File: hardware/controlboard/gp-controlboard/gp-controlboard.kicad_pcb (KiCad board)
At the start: 2 copper layers, 120 x 50 mm, 11 parts

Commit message: .
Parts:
- removed the VAL** at (145.0, 95.0)
- added VAL**: BUTTON-WE-430162073826, BUTTON:BUTTON-WE-430162073826, F.Cu at (110.0, 110.0)
- added VAL**: BUTTON-WE-430162073826, BUTTON:BUTTON-WE-430162073826, F.Cu at (150.0, 95.0)
- added VAL**: BUTTON-WE-430162073826, BUTTON:BUTTON-WE-430162073826, F.Cu at (150.0, 110.0)
- added VAL**: BUTTON-WE-430162073826, BUTTON:BUTTON-WE-430162073826, F.Cu at (110.0, 80.0)
- added VAL**: BUTTON-WE-430162073826, BUTTON:BUTTON-WE-430162073826, F.Cu at (150.0, 80.0)
- moved VAL** 20.0 mm to (205.0, 80.0)
- moved VAL** 20.0 mm to (225.0, 110.0)
- moved VAL** 20.0 mm to (225.0, 95.0)
- moved VAL** 20.0 mm to (225.0, 80.0)
- moved VAL** 20.0 mm to (205.0, 110.0)
- moved VAL** 20.0 mm to (205.0, 95.0)
- moved REF** 8.56 mm to (173.6, 79.7)
- moved VAL** 5.00 mm to (110.0, 95.0)
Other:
- board size 120 x 50 mm -> 140 x 50 mm

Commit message: Started PCB
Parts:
- removed REF**: ESP32-WROOM-32D, WIFI:ESP32-WROOM-32D
- added C101: 4u7, CAPACITOR:CAPACITOR-1206, F.Cu at (-79.5, 44.5)
- added C102: 4u7, CAPACITOR:CAPACITOR-1206, F.Cu at (-18.7, 16.3)
- added C103: 1u, CAPACITOR:CAPACITOR-1206, F.Cu at (-24.1, 16.3)
- added C104: 1u, CAPACITOR:CAPACITOR-1206, F.Cu at (-29.6, 16.3)
- added C105: 100n, CAPACITOR:CAPACITOR-0805, F.Cu at (-31.2, 40.7)
- added C106: 10u, CAPACITOR:CAPACITOR-1206, F.Cu at (-74.0, 44.5)
- added C107: 100n, CAPACITOR:CAPACITOR-0805, F.Cu at (-8.47, 17.2)
- added C108: 100n, CAPACITOR:CAPACITOR-0805, F.Cu at (3.18, 5.13)
- added D101: MBRA340T3G, DIODE:DIODE-DO214AC-UNI, F.Cu at (-92.4, 44.9)
- added DL101: GREEN, LEDs:LED-0805, F.Cu at (-1.07, 2.08)
- added DL102: RED, LEDs:LED-0805, F.Cu at (-12.1, 14.2)
- added DL103: RED, LEDs:LED-0805, F.Cu at (-31.2, 34.6)
- added DL104: GREEN, LEDs:LED-0805, F.Cu at (-12.1, 11.1)
- added P101: BATTERY, CONNECTOR_MPT:CONN-MPT0.5_2-2.54, F.Cu at (190.0, 134.0)
- added P102: EN_JMP, CONNECTOR:CONN-STRIP-2x1-2.54, F.Cu at (-66.1, 11.7)
- added P103: NUCLEO-CN3, CONNECTOR:SOCKET_16x1_2.54_SMD-WE-61001611921, F.Cu at (183.0, 115.0)
- added P104: NUCLEO-CN4, CONNECTOR:SOCKET_16x1_2.54_SMD-WE-61001611921, F.Cu at (167.8, 115.0)
- added P105: ESP_PROG, CONNECTOR:CONN-STRIP-3x1-2.54, F.Cu at (-100.9, 44.8)
- added P106: BOOT_JMP, CONNECTOR:CONN-STRIP-2x1-2.54, F.Cu at (-66.1, 15.8)
- added R101: 330, RESISTOR:RESISTOR-0805, F.Cu at (-13.1, 21.5)
- added R102: 270, RESISTOR:RESISTOR-0805, F.Cu at (-7.27, 14.2)
- added R103: 270, RESISTOR:RESISTOR-0805, F.Cu at (-3.02, 11.1)
- added R104: TBD, RESISTOR:RESISTOR-0805, F.Cu at (-26.9, 37.7)
- added R105: 330, RESISTOR:RESISTOR-0805, F.Cu at (-31.2, 37.7)
- added R106: 10k, RESISTOR:RESISTOR-0805, F.Cu at (-26.3, 34.6)
- added R107: TBD, RESISTOR:RESISTOR-0805, F.Cu at (-1.07, 5.13)
- added R108: TBD, RESISTOR:RESISTOR-0805, F.Cu at (-7.27, 11.1)
- added SW101: 430162073826, BUTTON:BUTTON-WE-430162073826, F.Cu at (-24.3, 26.1)
- added SW102: 430162073826, BUTTON:BUTTON-WE-430162073826, F.Cu at (-42.3, 40.1)
- added SW103: 430162073826, BUTTON:BUTTON-WE-430162073826, F.Cu at (-5.22, -6.47)
- added SW104: 430162073826, BUTTON:BUTTON-WE-430162073826, F.Cu at (-23.3, 7.58)
- added SW105: 430162073826, BUTTON:BUTTON-WE-430162073826, F.Cu at (-42.3, 26.1)
- added SW106: 430162073826, BUTTON:BUTTON-WE-430162073826, F.Cu at (-60.4, 40.1)
- added SW107: 430162073826, BUTTON:BUTTON-WE-430162073826, F.Cu at (-23.3, -6.47)
- added SW108: 430162073826, BUTTON:BUTTON-WE-430162073826, F.Cu at (-78.4, 35.7)
- added SW109: 430162073826, BUTTON:BUTTON-WE-430162073826, F.Cu at (-60.4, 26.1)
- added SW110: 430162073826, BUTTON:BUTTON-WE-430162073826, F.Cu at (-96.5, 35.7)
- added SW111: 430162073826, BUTTON:BUTTON-WE-430162073826, F.Cu at (-78.4, 21.7)
- added SW112: 450405020524, SWITCH:SWITCH-SPDT-WURTH-450405020524, F.Cu at (-8.72, 5.08)
- added SW113: 430162073826, BUTTON:BUTTON-WE-430162073826, F.Cu at (-96.5, 21.7)
- added SW114: 430162073826, BUTTON:BUTTON-WE-430162073826, F.Cu at (-78.4, 7.63)
- added SW115: 430162073826, BUTTON:BUTTON-WE-430162073826, F.Cu at (-96.5, 7.63)
- added U101: STBC08PMR, DFN:DFN6_3.0x3.0_1.0, F.Cu at (-84.9, 45.1)
- added U102: TLV70233DBV, SOT:SOT23-5, F.Cu at (-12.9, 17.8)
- added U103: ESP32-WROOM-32E(8MB), WIFI:ESP32-WROOM-32D, F.Cu at (175.0, 80.0)
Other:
- board size 140 x 50 mm -> 140 x 70 mm

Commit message: Working on PCB, placed almost all the components
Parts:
- moved P105 291.5 mm to (188.4, 80.6), turned to 270 degrees
- moved U101 284.8 mm to (188.5, 124.8), turned to 90 degrees
- moved C101 278.1 mm to (188.5, 119.0)
- moved D101 276.8 mm to (174.2, 119.2), turned to 90 degrees
- moved P106 265.0 mm to (188.4, 89.6), turned to 270 degrees
- moved DL103 243.6 mm to (194.5, 126.2), turned to 270 degrees
- moved P102 237.3 mm to (161.6, 78.6), turned to 90 degrees
- moved C106 236.8 mm to (161.0, 73.2), turned to 270 degrees
- moved C102 235.6 mm to (188.5, 128.5)
- moved DL102 233.3 mm to (192.5, 126.2), turned to 270 degrees
- moved R104 232.1 mm to (189.5, 121.5)
- moved C104 232.0 mm to (175.8, 124.2)
- moved C103 230.3 mm to (175.8, 130.8)
- moved R102 227.4 mm to (192.5, 122.8), turned to 270 degrees
- moved SW112 227.0 mm to (175.2, 138.0)
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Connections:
- D101 pad 1: Net-(C104-Pad1) -> +3.3V
- D101 pad 2: +3.3V -> Net-(C104-Pad1)
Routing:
- net +VBAT: track 0.00 -> 15.2 mm

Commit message: Place buttons
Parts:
- removed VAL** (x14): BUTTON-WE-430162073826, BUTTON:BUTTON-WE-430162073826
- moved SW115 344.0 mm to (225.0, 130.0)
- moved SW113 326.7 mm to (225.0, 80.0)
- moved SW114 318.7 mm to (225.0, 105.0)
- moved SW110 309.3 mm to (205.0, 105.0)
- moved SW111 303.4 mm to (205.0, 130.0)
- moved SW109 270.8 mm to (205.0, 80.0)
- moved SW108 247.1 mm to (150.0, 130.0)
- moved SW106 214.1 mm to (150.0, 80.0)
- moved SW107 206.0 mm to (150.0, 105.0)
- moved SW105 201.2 mm to (130.0, 130.0)
- moved SW103 178.6 mm to (110.0, 130.0)
- moved SW104 169.5 mm to (130.0, 80.0)
- moved SW102 165.6 mm to (110.0, 105.0)
- moved SW101 144.7 mm to (110.0, 80.0)

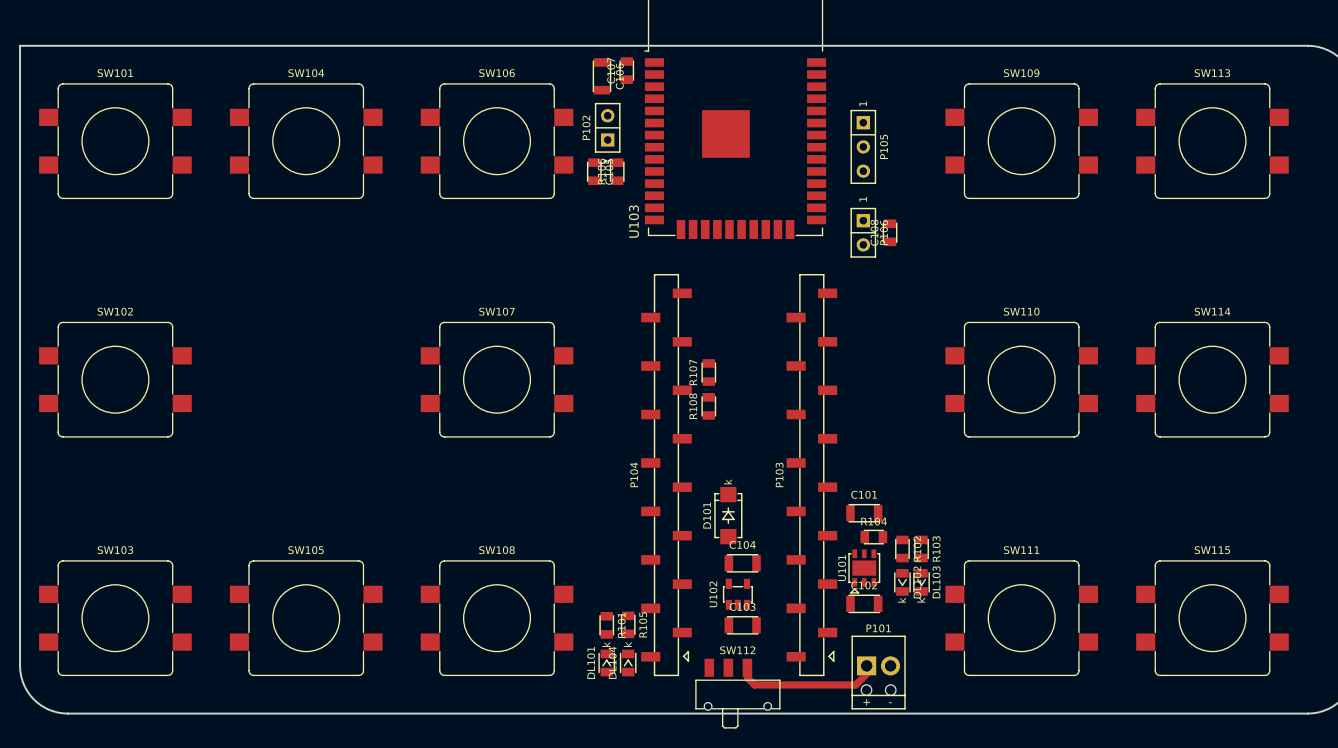
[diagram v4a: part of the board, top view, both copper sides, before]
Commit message: Added connection to nucleo board. Working on PCB
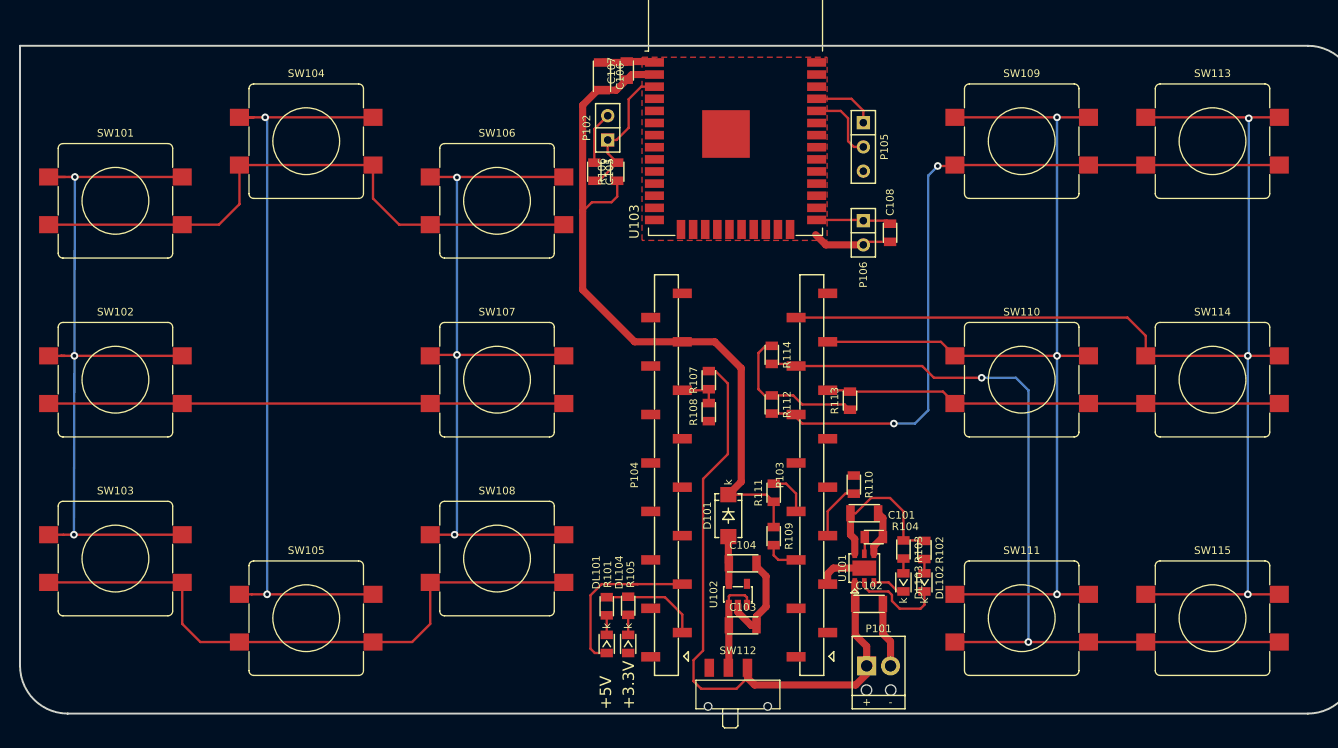
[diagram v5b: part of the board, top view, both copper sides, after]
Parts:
- added G***: LOGO, LOGO:LOGO_NOWAE_40MM_FSILK, B.Cu at (174.4, 112.2)
- added G***: LOGO, EXTLOGO:GIAMMABOT_35MM_FSILK, B.Cu at (174.4, 96.8)
- added R109: 10k, RESISTOR:RESISTOR-0805, F.Cu at (179.0, 121.4)
- added R110: 10k, RESISTOR:RESISTOR-0805, F.Cu at (187.4, 116.0)
- added R111: 10k, RESISTOR:RESISTOR-0805, F.Cu at (179.0, 116.8)
- added R112: 10k, RESISTOR:RESISTOR-0805, F.Cu at (178.8, 107.6)
- added R113: 10k, RESISTOR:RESISTOR-0805, F.Cu at (187.0, 107.2)
- added R114: 10k, RESISTOR:RESISTOR-0805, F.Cu at (178.8, 102.4)
- moved SW101 6.25 mm to (110.0, 86.2)
- moved SW103 6.25 mm to (110.0, 123.8)
- moved SW106 6.25 mm to (150.0, 86.2)
- moved SW108 6.25 mm to (150.0, 123.8)
- moved R102 2.30 mm to (194.8, 122.8)
- moved DL102 2.30 mm to (194.8, 126.2)
- moved DL101 2.00 mm to (161.5, 132.7)
- moved DL104 2.00 mm to (163.8, 132.7)
- moved R101 2.00 mm to (161.5, 128.8)
- moved R105 2.00 mm to (163.8, 128.7)
- moved R103 1.90 mm to (192.6, 122.8)
- moved DL103 1.90 mm to (192.6, 126.2)
- moved R107 0.80 mm to (172.2, 105.0)
- moved R108 0.60 mm to (172.2, 108.4)
- moved C102 0.50 mm to (189.0, 128.5)
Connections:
- net /ESP2MCU_03 renamed Net-(U103-Pad29)
- net /ESP2MCU_04 renamed Net-(U103-Pad26)
- net Net-(P104-Pad10) renamed /ADDR_2
- net Net-(P104-Pad8) renamed /ADDR_0
- net Net-(P104-Pad9) renamed /ADDR_1
- P103 pad 1: Net-(P103-Pad1) -> /UART_CMD_TX
- P103 pad 10: Net-(P103-Pad10) -> /DIRECTION_C3
- P103 pad 11: Net-(P103-Pad11) -> /POWER_R1
- P103 pad 12: Net-(P103-Pad12) -> /POWER_R2
- P103 pad 13: Net-(P103-Pad13) -> /POWER_R3
- P103 pad 14: Net-(P103-Pad14) -> /POWER_C1
- P103 pad 15: Net-(P103-Pad15) -> /POWER_C2
- P103 pad 2: Net-(P103-Pad2) -> /UART_CMD_RX
- P103 pad 5: Net-(P103-Pad5) -> /DIRECTION_R1
- P103 pad 6: Net-(P103-Pad6) -> /DIRECTION_R2
- P103 pad 7: Net-(P103-Pad7) -> /DIRECTION_R3
- P103 pad 8: Net-(P103-Pad8) -> /DIRECTION_C1
- P103 pad 9: Net-(P103-Pad9) -> /DIRECTION_C2
- P104 pad 6: Net-(P104-Pad6) -> /ESP2MCU_01
- P104 pad 7: Net-(P104-Pad7) -> /ESP2MCU_02
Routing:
- net /POWER_C2: track 0.00 -> 131.6 mm, vias 0 -> 3
- net /POWER_C1: track 0.00 -> 105.9 mm, vias 0 -> 3
- net +3.3V: track 0.00 -> 91.7 mm
- net /POWER_R3: track 0.00 -> 88.4 mm, vias 0 -> 2
- net /DIRECTION_C1: track 0.00 -> 81.7 mm, vias 0 -> 3
- net /DIRECTION_C3: track 0.00 -> 79.8 mm, vias 0 -> 3
- net /DIRECTION_C2: track 0.00 -> 79.6 mm, vias 0 -> 2
- net /POWER_R1: track 0.00 -> 79.4 mm, vias 0 -> 2
- net /DIRECTION_R3: track 0.00 -> 68.9 mm
- net /DIRECTION_R1: track 0.00 -> 67.2 mm
- net /DIRECTION_R2: track 0.00 -> 60.1 mm
- net GND: track 0.00 -> 57.0 mm
- net +VBAT: track 15.2 -> 66.1 mm
- net /POWER_R2: track 0.00 -> 47.9 mm
- net +5V: track 0.00 -> 34.7 mm
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- added copper zone on F.Cu, net GND
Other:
- board text added: "+3.3V"
- board text added: "+5V"
- board text added: "SPONSORED BY"

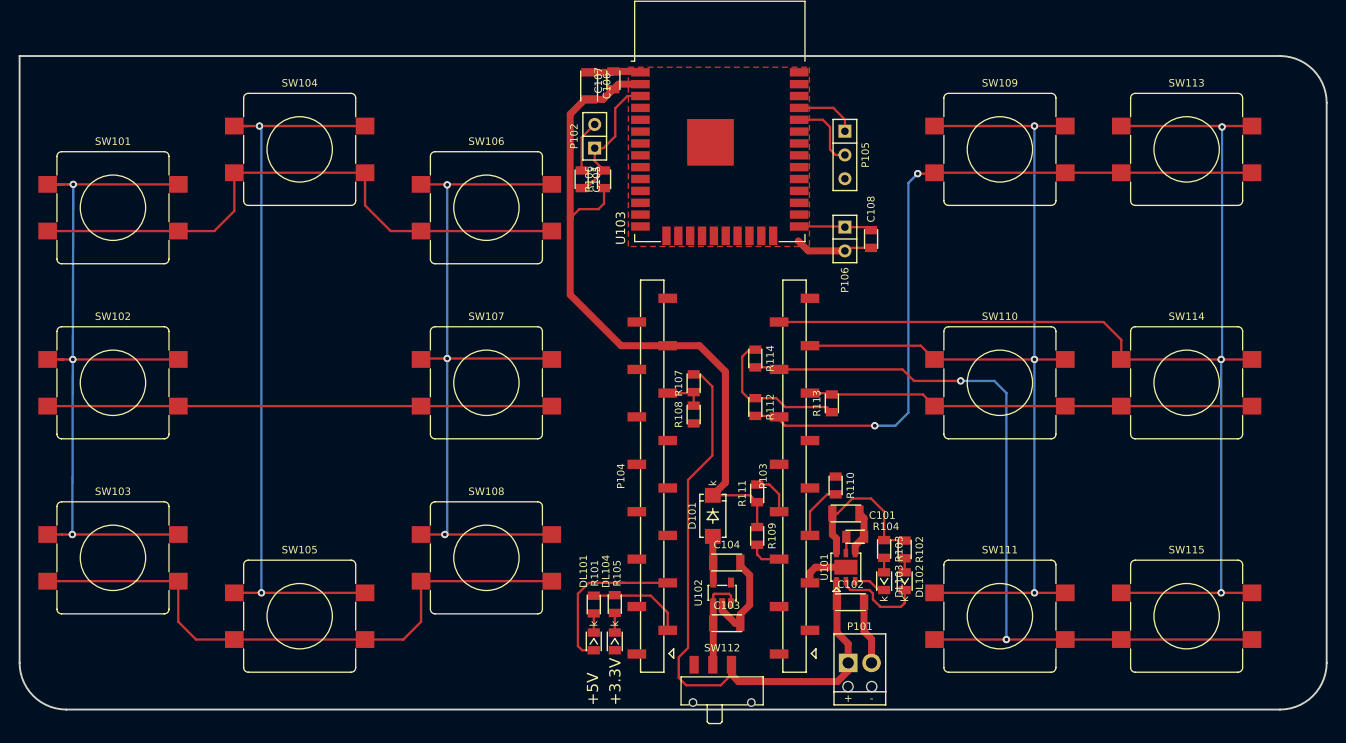
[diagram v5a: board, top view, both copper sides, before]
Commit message: Added jumper for board address into control board. Ended PCB
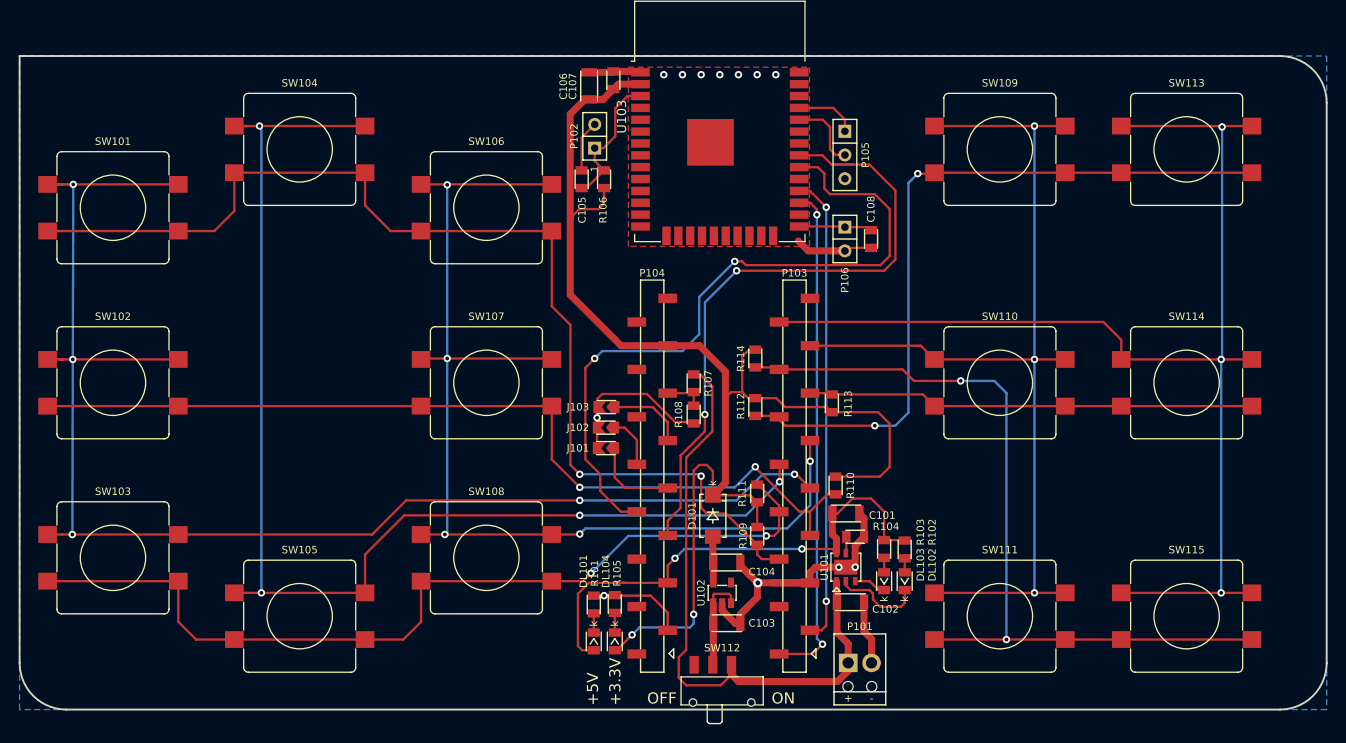
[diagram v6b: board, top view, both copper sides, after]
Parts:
- added J101: JUMPER-2_1, MISC:JUMPERSMD-2-0805, F.Cu at (162.8, 112.0)
- added J102: JUMPER-2_1, MISC:JUMPERSMD-2-0805, F.Cu at (162.8, 109.8)
- added J103: JUMPER-2_1, MISC:JUMPERSMD-2-0805, F.Cu at (162.8, 107.6)
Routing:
- net /ESP2MCU_02: track 0.00 -> 76.4 mm, vias 0 -> 2
- net /DIRECTION_C1: track 81.7 -> 152.6 mm, vias 3 -> 5
- net /ESP2MCU_01: track 0.00 -> 70.4 mm, vias 0 -> 2
- net /UART_CMD_TX: track 0.00 -> 54.1 mm, vias 0 -> 2
- net /DIRECTION_C2: track 79.6 -> 133.2 mm, vias 2 -> 4
- net /DIRECTION_R1: track 67.2 -> 118.6 mm, vias 0 -> 2
- net +3.3V: track 91.7 -> 142.5 mm, vias 0 -> 2
- net /UART_CMD_RX: track 0.00 -> 50.4 mm, vias 0 -> 2
- net /DIRECTION_R2: track 60.1 -> 97.6 mm, vias 0 -> 2
- net /DIRECTION_C3: track 79.8 -> 115.7 mm, vias 3 -> 5
- net GND: track 57.0 -> 88.8 mm, vias 0 -> 12
- net /DIRECTION_R3: track 68.9 -> 96.8 mm, vias 0 -> 2
- net +5V: track 34.7 -> 55.5 mm, vias 0 -> 2
- net /ADDR_0: track 0.00 -> 9.28 mm
- net /ADDR_2: track 0.00 -> 8.26 mm
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- added copper zone on B.Cu, net GND
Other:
- board text added: "GB-CONTROLBOARD REV. 0"
- board text added: "OFF"
- board text added: "ON"
